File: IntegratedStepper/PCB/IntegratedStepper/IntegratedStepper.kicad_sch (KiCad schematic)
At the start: 0 parts

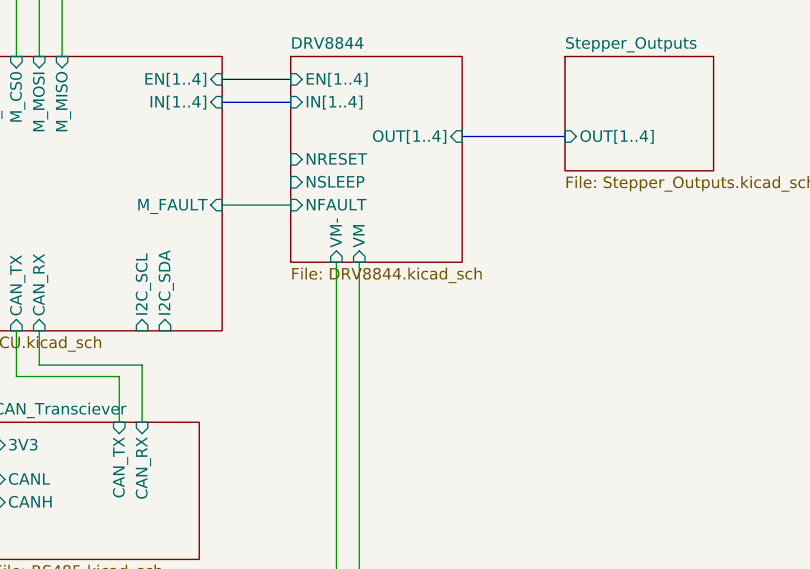
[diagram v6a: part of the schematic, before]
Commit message: Update schem + PCB with learnings from bringup
PU resistors for DRV8844 were on a 3V3 island and were NOT pulled up :L
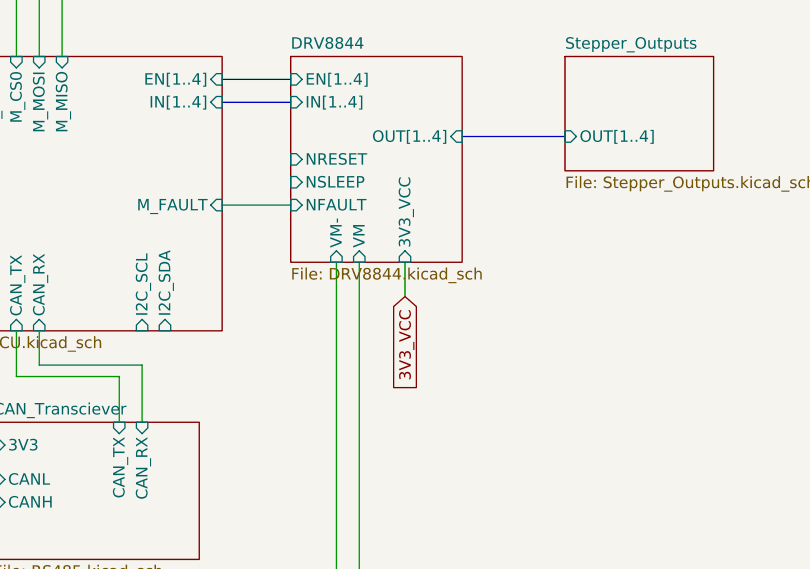
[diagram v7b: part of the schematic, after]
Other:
- sheet DRV8844 ports: added 3V3_VCC; removed none
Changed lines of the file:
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@@
+	(wire
+		(pts
+			(xy 161.29 93.98) (xy 161.29 97.79)
+		)
+		(stroke
+			(width 0)
+			(type default)
+		)
+	)
 	(wire
 		(pts
@@
 			(width 0)
 			(type default)
+		)
+	)
+	(global_label "3V3_VCC"
+		(shape input)
+		(at 161.29 97.79 270)
+		(fields_autoplaced yes)
+		(effects
+			(font
+				(size 1.27 1.27)
+			)
+			(justify right)
+		)
+		(property "Intersheetrefs" "${INTERSHEET_REFS}"
+			(at 161.29 108.879 90)
+			(effects
+				(font
+					(size 1.27 1.27)
+				)
+				(justify right)
+				(hide yes)
+			)
 		)
 	)
@@
 			)
 		)
+		(pin "3V3_VCC" input
+			(at 161.29 93.98 270)
+			(effects
+				(font
+					(size 1.27 1.27)
+				)
+				(justify left)
+			)
+		)
